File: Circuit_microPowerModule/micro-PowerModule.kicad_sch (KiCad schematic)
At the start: 5 parts, among them SW1 RotaryEncoder_Switch, U1 INA219BxD, U2 MAX485E, U3 MCP4725xxx-xCH, U4 MT3608

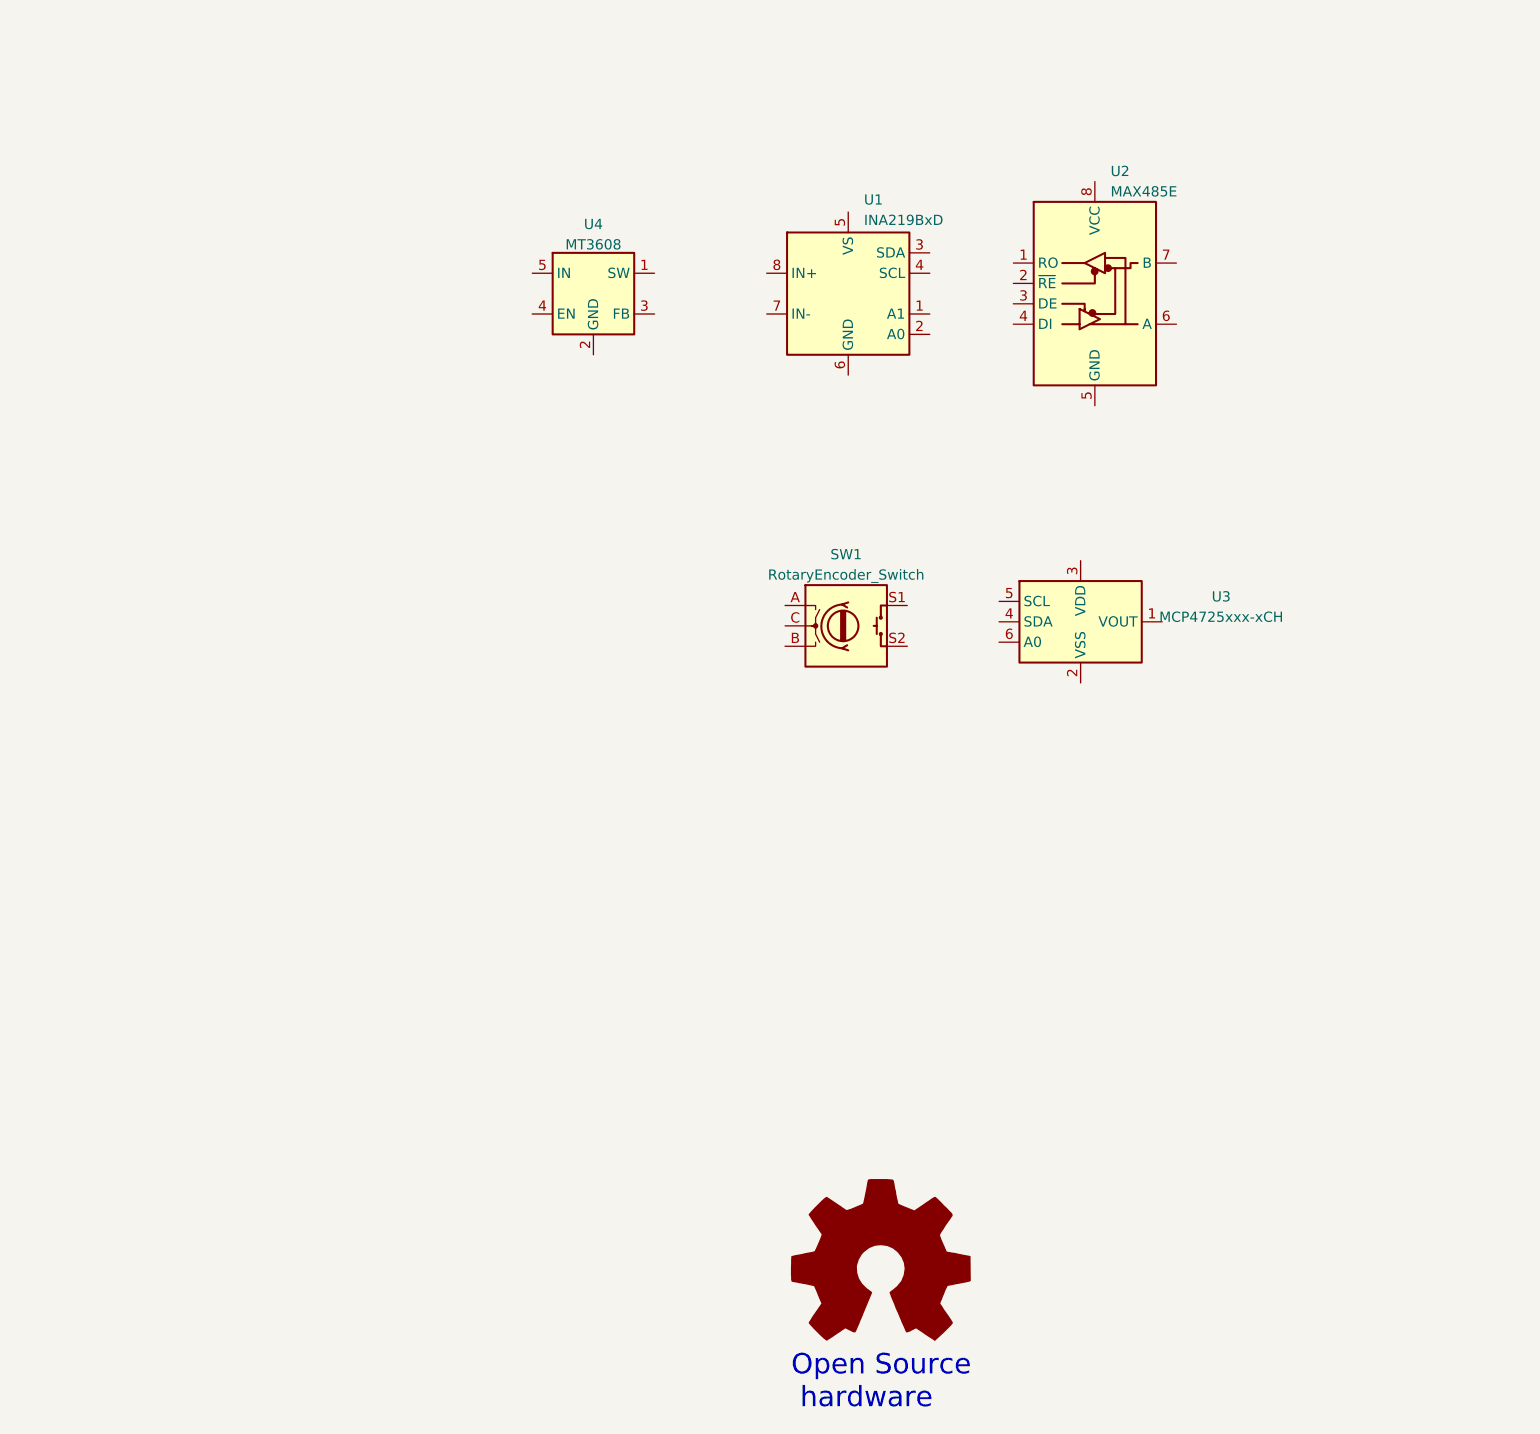
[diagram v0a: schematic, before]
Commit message: decision MCU-RP2040
added RP2040 to circuit
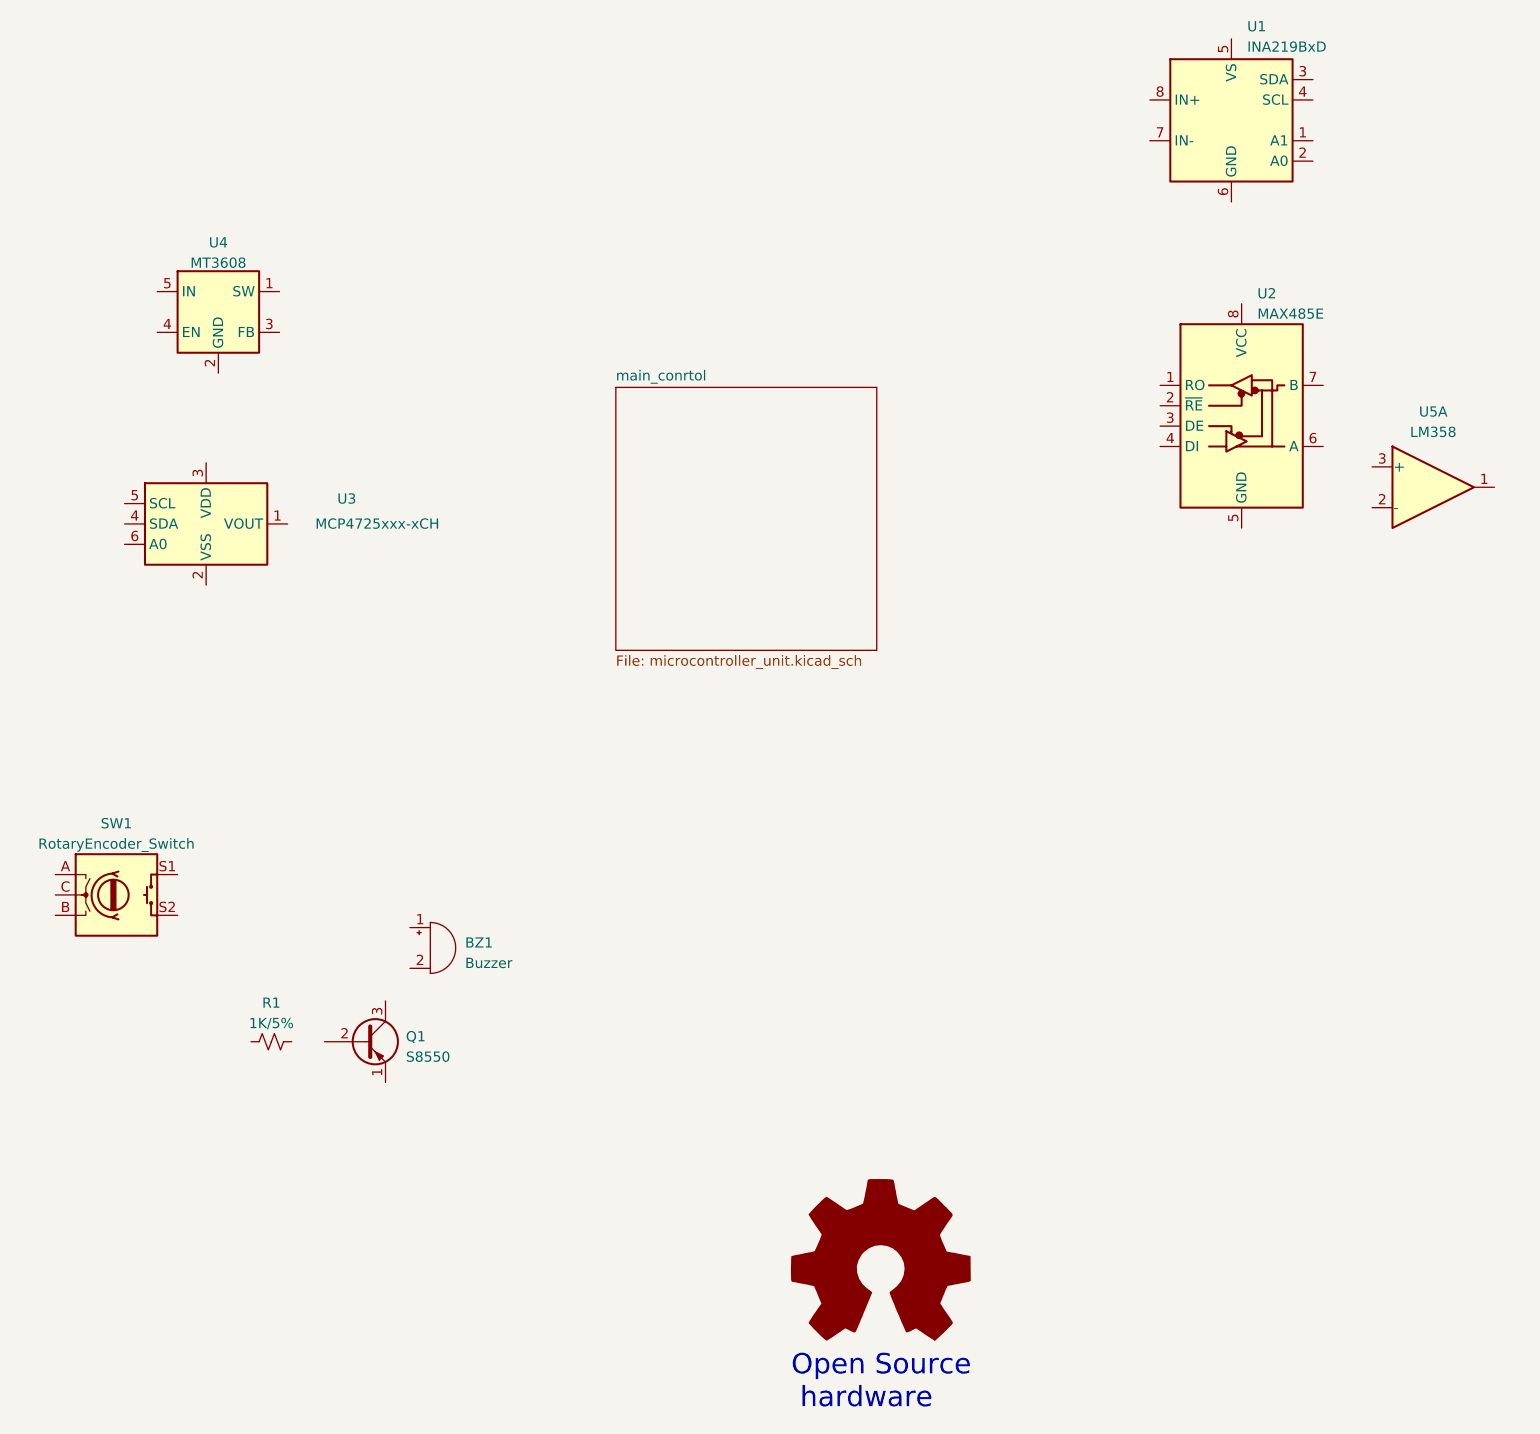
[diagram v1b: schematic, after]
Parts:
- added BZ1: Buzzer, symbol Device:Buzzer
- added Q1: S8550, Package_TO_SOT_THT:TO-92_Inline, symbol Transistor_BJT:S8550
- added R1: 1K/5%, Resistor_SMD:R_0603_1608Metric, symbol Device:R_Small_US
- added U5: LM358, symbol Amplifier_Operational:LM358
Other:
- added sheet main_conrtol (microcontroller_unit.kicad_sch)
- moved on the sheet: SW1, U1, U2, U3, U4

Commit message: added MP2315S lib, updated circuit
updated block diagram by-sa
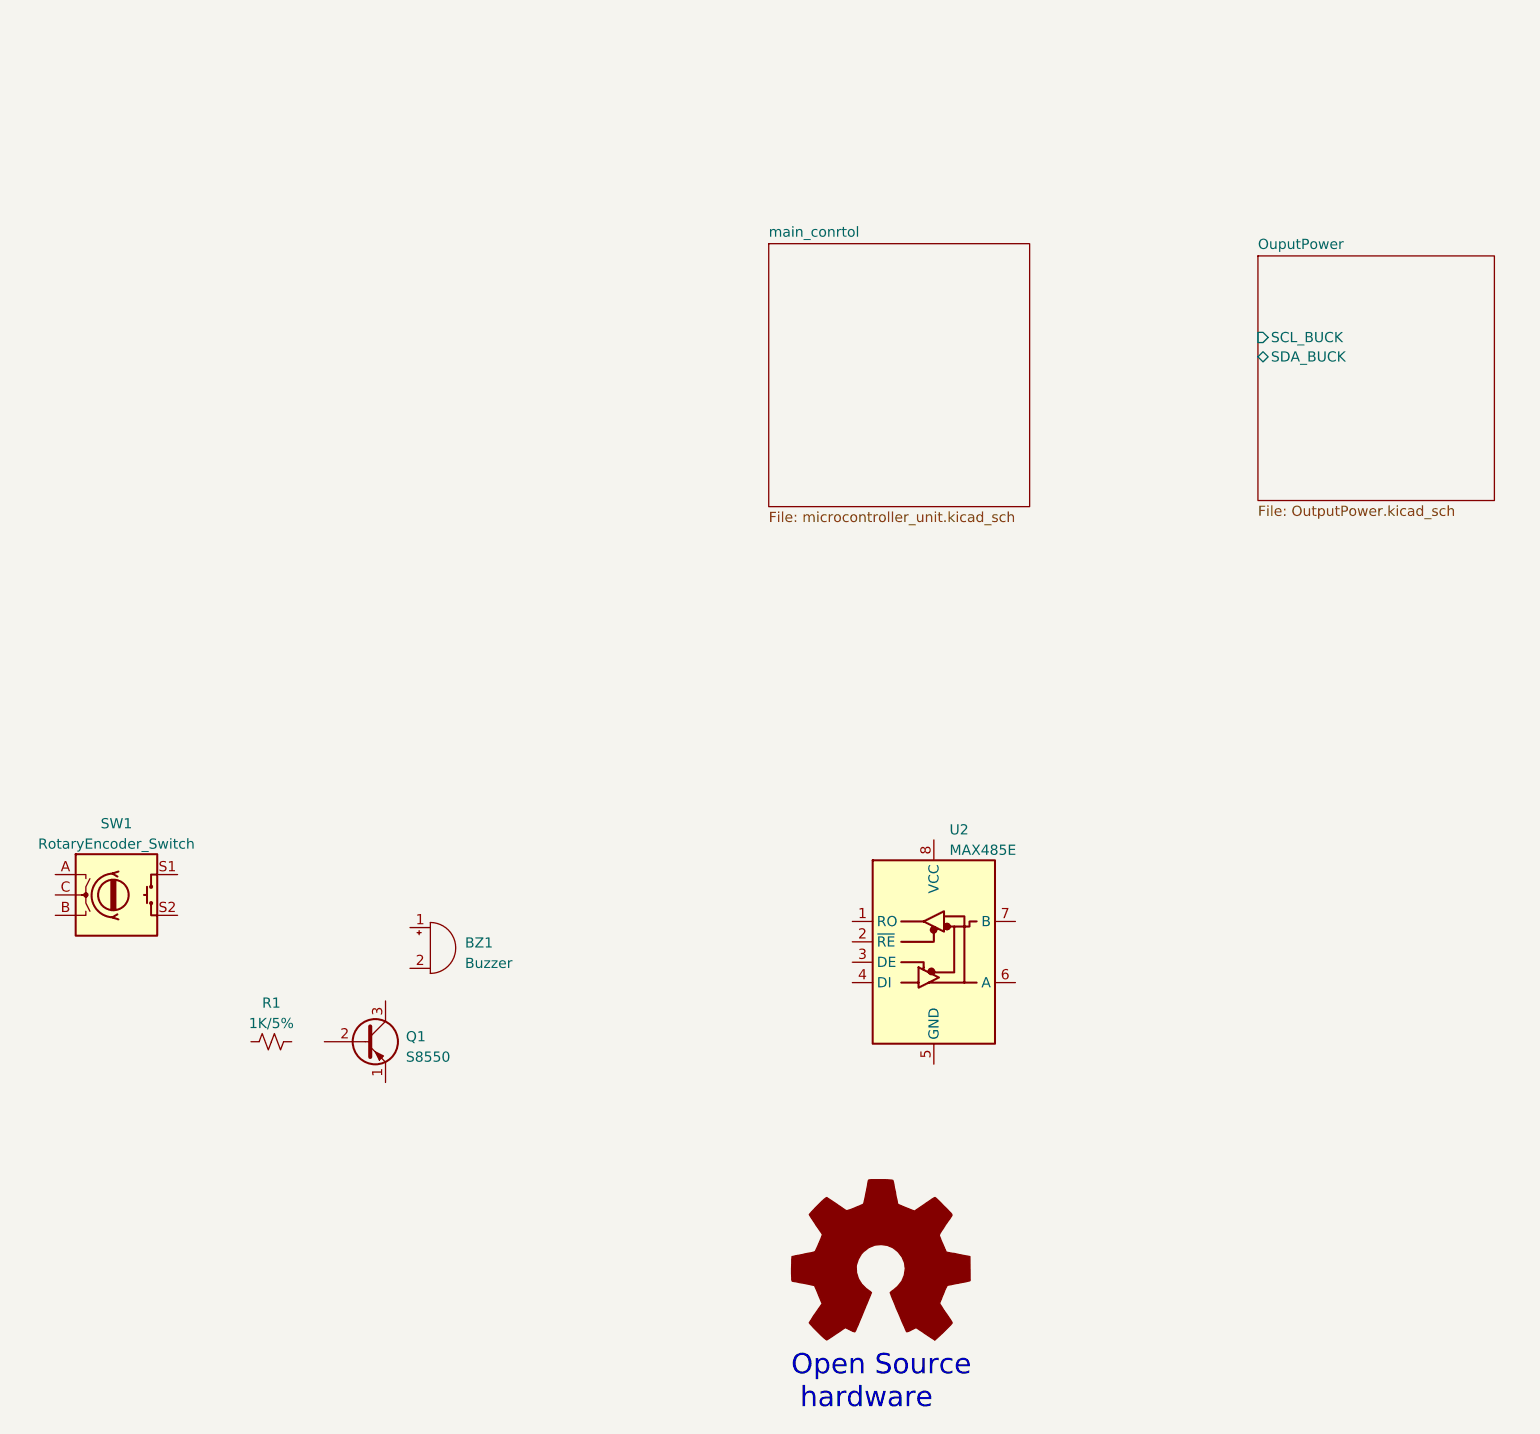
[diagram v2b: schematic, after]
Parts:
- removed U1: INA219BxD, Package_SO:SOIC-8_3.9x4.9mm_P1.27mm, symbol Sensor_Energy:INA219BxD
- removed U3: MCP4725xxx-xCH, Package_TO_SOT_SMD:SOT-23-6, symbol Analog_DAC:MCP4725xxx-xCH
- removed U4: MT3608, Package_TO_SOT_SMD:SOT-23-6, symbol Regulator_Switching:MT3608
- removed U5: LM358, symbol Amplifier_Operational:LM358
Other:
- added sheet OuputPower (OutputPower.kicad_sch)
- moved on the sheet: U2
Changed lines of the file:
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@@
     (effects (font (face "Monaco") (size 2.54 2.54) (color 132 0 0 1)) (justify left bottom))
-  )
-  (symbol (lib_id "Regulator_Switching:MT3608") (at 77.724 60.452 0) (unit 1)
-    (in_bom yes) (on_board yes) (dnp no)
-    (property "Reference" "U4" (at 77.724 51.816 0)
-      (effects (font (size 1.27 1.27)))
-    )
-    (property "Value" "MT3608" (at 77.724 54.356 0)
-      (effects (font (size 1.27 1.27)))
-    )
-    (property "Footprint" "Package_TO_SOT_SMD:SOT-23-6" (at 78.994 66.802 0)
-      (effects (font (size 1.27 1.27) italic) (justify left) hide)
-    )
-    (property "Datasheet" "https://www.olimex.com/Products/Breadboarding/BB-PWR-3608/resources/MT3608.pdf" (at 71.374 49.022 0)
-      (effects (font (size 1.27 1.27)) hide)
-    )
-    (pin "1")
-    (pin "2")
-    (pin "3")
-    (pin "4")
-    (pin "5")
-    (pin "6")
-    (instances
-      (project "micro-PowerModule"
-        (path "/38b19d1a-a8d3-49c0-a6a2-bee4e845832f"
-          (reference "U4") (unit 1)
-        )
-      )
-    )
   )
   (symbol (lib_id "Transistor_BJT:S8550") (at 96.012 151.384 0) (unit 1)
@@
     )
   )
-  (symbol (lib_id "Amplifier_Operational:LM358") (at 229.108 82.296 0) (unit 1)
-    (in_bom yes) (on_board yes) (dnp no) (fields_autoplaced)
-    (property "Reference" "U5" (at 229.108 72.898 0)
-      (effects (font (size 1.27 1.27)))
-    )
-    (property "Value" "LM358" (at 229.108 75.438 0)
-      (effects (font (size 1.27 1.27)))
-    )
-    (property "Footprint" "" (at 229.108 82.296 0)
-      (effects (font (size 1.27 1.27)) hide)
-    )
-    (property "Datasheet" "http://www.ti.com/lit/ds/symlink/lm2904-n.pdf" (at 229.108 82.296 0)
-      (effects (font (size 1.27 1.27)) hide)
-    )
-    (pin "1")
-    (pin "2")
-    (pin "3")
-    (pin "5")
-    (pin "6")
-    (pin "7")
-    (pin "4")
-    (pin "8")
-    (instances
-      (project "micro-PowerModule"
-        (path "/38b19d1a-a8d3-49c0-a6a2-bee4e845832f"
-          (reference "U5") (unit 1)
-        )
-      )
-    )
-  )
-  (symbol (lib_id "Analog_DAC:MCP4725xxx-xCH") (at 76.2 86.868 0) (unit 1)
-    (in_bom yes) (on_board yes) (dnp no)
-    (property "Reference" "U3" (at 93.726 83.7439 0)
-      (effects (font (size 1.27 1.27)))
-    )
-    (property "Value" "MCP4725xxx-xCH" (at 97.536 86.868 0)
-      (effects (font (size 1.27 1.27)))
-    )
-    (property "Footprint" "Package_TO_SOT_SMD:SOT-23-6" (at 76.2 93.218 0)
-      (effects (font (size 1.27 1.27)) hide)
-    )
-    (property "Datasheet" "http://ww1.microchip.com/downloads/en/DeviceDoc/22039d.pdf" (at 76.2 86.868 0)
-      (effects (font (size 1.27 1.27)) hide)
-    )
-    (pin "1")
-    (pin "2")
-    (pin "3")
-    (pin "4")
-    (pin "5")
-    (pin "6")
-    (instances
-      (project "micro-PowerModule"
-        (path "/38b19d1a-a8d3-49c0-a6a2-bee4e845832f"
-          (reference "U3") (unit 1)
-        )
-      )
-    )
-  )
-  (symbol (lib_id "Sensor_Energy:INA219BxD") (at 203.962 36.576 0) (unit 1)
-    (in_bom yes) (on_board yes) (dnp no) (fields_autoplaced)
-    (property "Reference" "U1" (at 205.9179 24.892 0)
-      (effects (font (size 1.27 1.27)) (justify left))
-    )
-    (property "Value" "INA219BxD" (at 205.9179 27.432 0)
-      (effects (font (size 1.27 1.27)) (justify left))
-    )
-    (property "Footprint" "Package_SO:SOIC-8_3.9x4.9mm_P1.27mm" (at 224.282 45.466 0)
-      (effects (font (size 1.27 1.27)) hide)
-    )
-    (property "Datasheet" "http://www.ti.com/lit/ds/symlink/ina219.pdf" (at 212.852 39.116 0)
-      (effects (font (size 1.27 1.27)) hide)
-    )
-    (pin "1")
-    (pin "2")
-    (pin "3")
-    (pin "4")
-    (pin "5")
-    (pin "6")
-    (pin "7")
-    (pin "8")
-    (instances
-      (project "micro-PowerModule"
-        (path "/38b19d1a-a8d3-49c0-a6a2-bee4e845832f"
-          (reference "U1") (unit 1)
-        )
-      )
-    )
-  )
   (symbol (lib_id "Device:R_Small_US") (at 84.328 151.384 90) (unit 1)
     (in_bom yes) (on_board yes) (dnp no) (fields_autoplaced)
@@
     )
   )
-  (symbol (lib_id "Interface_UART:MAX485E") (at 205.232 72.136 0) (unit 1)
+  (symbol (lib_id "Interface_UART:MAX485E") (at 166.878 138.938 0) (unit 1)
     (in_bom yes) (on_board yes) (dnp no) (fields_autoplaced)
-    (property "Reference" "U2" (at 207.1879 58.166 0)
+    (property "Reference" "U2" (at 168.8339 124.968 0)
       (effects (font (size 1.27 1.27)) (justify left))
     )
-    (property "Value" "MAX485E" (at 207.1879 60.706 0)
+    (property "Value" "MAX485E" (at 168.8339 127.508 0)
       (effects (font (size 1.27 1.27)) (justify left))
     )
-    (property "Footprint" "" (at 205.232 89.916 0)
+    (property "Footprint" "" (at 166.878 156.718 0)
       (effects (font (size 1.27 1.27)) hide)
     )
-    (property "Datasheet" "https://datasheets.maximintegrated.com/en/ds/MAX1487E-MAX491E.pdf" (at 205.232 70.866 0)
+    (property "Datasheet" "https://datasheets.maximintegrated.com/en/ds/MAX1487E-MAX491E.pdf" (at 166.878 137.668 0)
       (effects (font (size 1.27 1.27)) hide)
     )
@@
     )
   )
-  (sheet (at 127.254 69.85) (size 32.512 32.766) (fields_autoplaced)
+  (sheet (at 207.264 53.467) (size 29.464 30.48) (fields_autoplaced)
     (stroke (width 0.1524) (type solid))
     (fill (color 0 0 0 0.0000))
-    (property "Sheetname" "main_conrtol" (at 127.254 69.1384 0)
+    (property "Sheetname" "OuputPower" (at 207.264 52.7554 0)
       (effects (font (size 1.27 1.27)) (justify left bottom))
     )
-    (property "Sheetfile" "microcontroller_unit.kicad_sch" (at 127.254 103.2006 0)
+    (property "Sheetfile" "OutputPower.kicad_sch" (at 207.264 84.5316 0)
       (effects (font (size 1.27 1.27)) (justify left top))
     )
+    (pin "SCL_BUCK" input (at 207.264 63.627 180)
+      (effects (font (size 1.27 1.27)) (justify left))
+    )
+    (pin "SDA_BUCK" bidirectional (at 207.264 66.04 180)
+      (effects (font (size 1.27 1.27)) (justify left))
+    )
+    (instances
+      (project "micro-PowerModule"
+        (path "/38b19d1a-a8d3-49c0-a6a2-bee4e845832f" (page "3"))
+      )
+    )
+  )
+  (sheet (at 146.304 51.943) (size 32.512 32.766) (fields_autoplaced)
+    (stroke (width 0.1524) (type solid))
+    (fill (color 0 0 0 0.0000))
+    (property "Sheetname" "main_conrtol" (at 146.304 51.2314 0)
+      (effects (font (size 1.27 1.27)) (justify left bottom))
+    )
+    (property "Sheetfile" "microcontroller_unit.kicad_sch" (at 146.304 85.2936 0)
+      (effects (font (size 1.27 1.27)) (justify left top))
+    )
